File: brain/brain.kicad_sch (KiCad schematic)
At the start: 6 parts, among them J0 BAR0, J1 BAR1, J2 I2C, J5 XTRA, SW1 RESET, U1 Elite-C

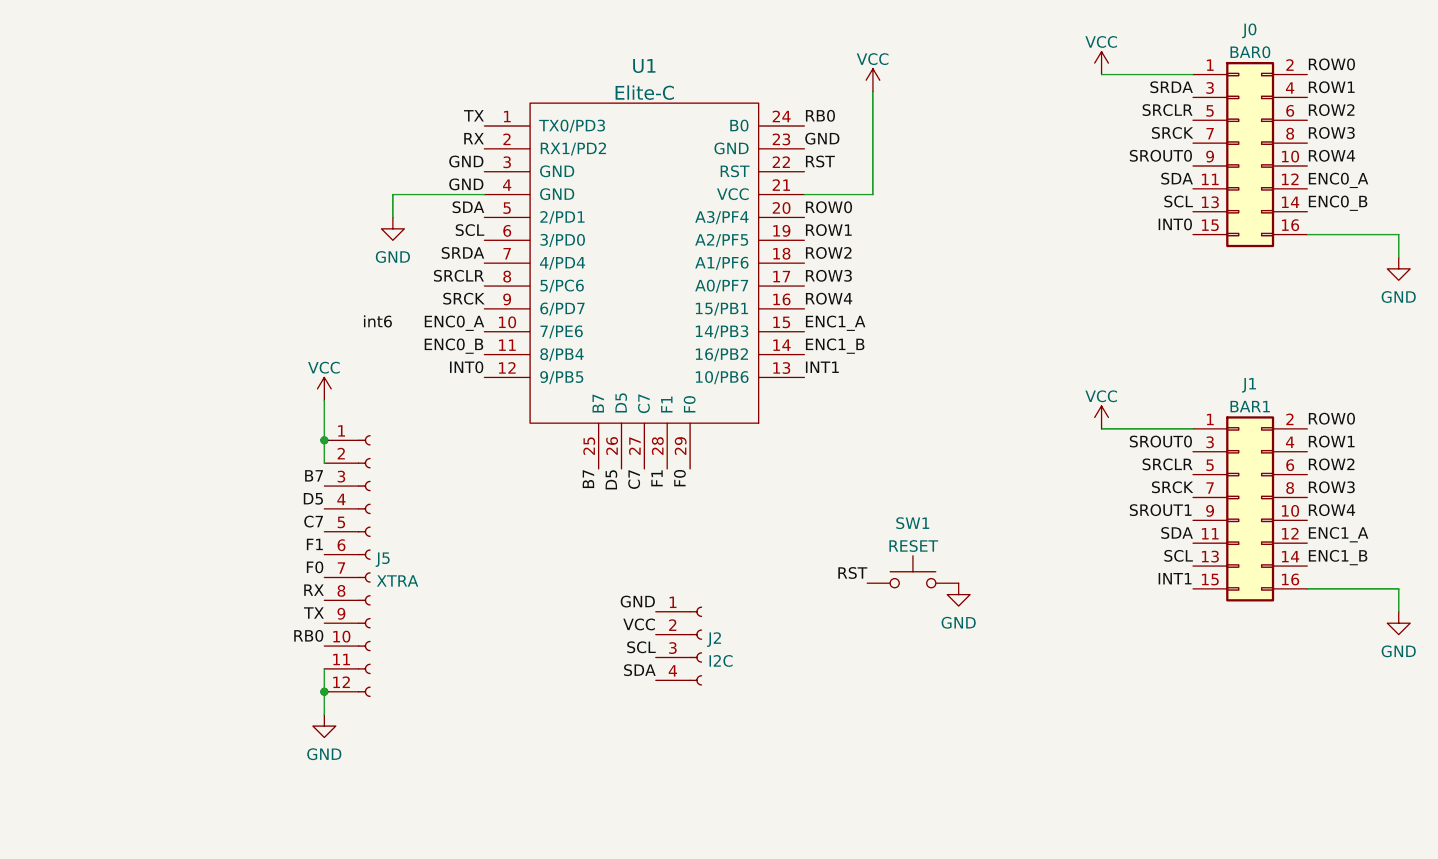
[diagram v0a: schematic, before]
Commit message: Use interrupt-enabled pins for encoder0 and int1
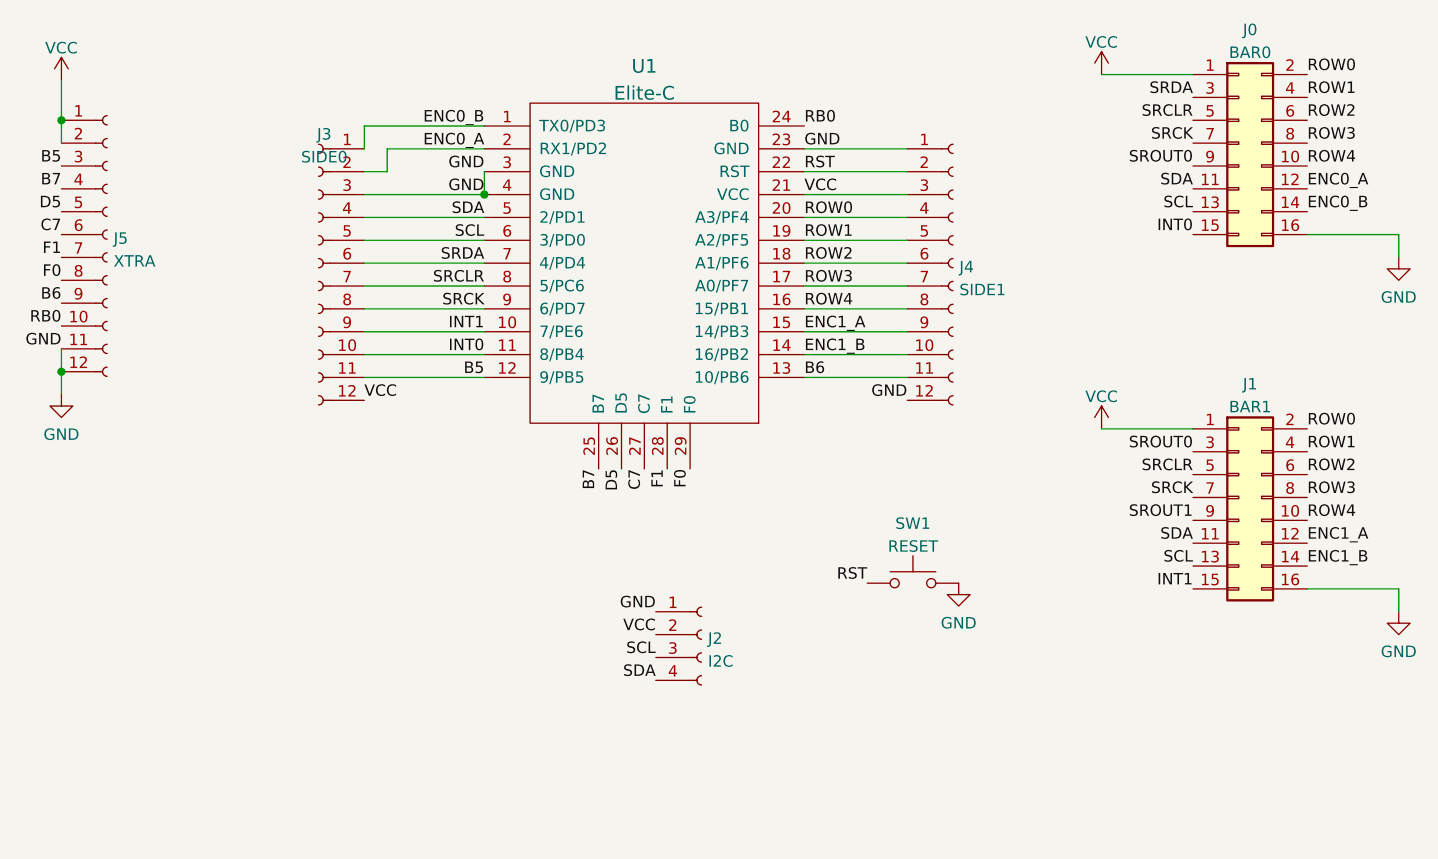
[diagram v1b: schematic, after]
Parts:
- added J3: SIDE0, Connector_PinSocket_2.54mm:PinSocket_1x12_P2.54mm_Vertical, symbol Connector:Conn_01x12_Female
- added J4: SIDE1, Connector_PinSocket_2.54mm:PinSocket_1x12_P2.54mm_Vertical, symbol Connector:Conn_01x12_Female
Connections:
- net B7: now also J5.4 (Pin_4); no longer J5.3 (Pin_3)
- net C7: now also J5.6 (Pin_6); no longer J5.5 (Pin_5)
- net D5: now also J5.5 (Pin_5); no longer J5.4 (Pin_4)
- net ENC0_A: now also U1.2 (RX1/PD2), J3.2 (Pin_2); no longer U1.10 (7/PE6)
- net ENC0_B: now also U1.1 (TX0/PD3), J3.1 (Pin_1); no longer U1.11 (8/PB4)
- net ENC1_A: now also J4.9 (Pin_9)
- net ENC1_B: now also J4.10 (Pin_10)
- net F0: now also J5.8 (Pin_8); no longer J5.7 (Pin_7)
- net F1: now also J5.7 (Pin_7); no longer J5.6 (Pin_6)
- net GND: now also J3.3 (Pin_3), J4.1 (Pin_1), J4.12 (Pin_12)
- net INT0: now also U1.11 (8/PB4), J3.10 (Pin_10); no longer U1.12 (9/PB5)
- net INT1: now also U1.10 (7/PE6), J3.9 (Pin_9); no longer U1.13 (10/PB6)
- net ROW0: now also J4.4 (Pin_4)
- net ROW1: now also J4.5 (Pin_5)
- net ROW2: now also J4.6 (Pin_6)
- net ROW3: now also J4.7 (Pin_7)
- net ROW4: now also J4.8 (Pin_8)
- net RST: now also J4.2 (Pin_2)
- net SCL: now also J3.5 (Pin_5)
- net SDA: now also J3.4 (Pin_4)
- net SRCK: now also J3.8 (Pin_8)
- net SRCLR: now also J3.7 (Pin_7)
- net SRDA: now also J3.6 (Pin_6)
- net VCC: now also J3.12 (Pin_12), J4.3 (Pin_3)
- removed net RX: J5.8 (Pin_8), U1.2 (RX1/PD2)
- net TX renamed B6
- net B6: now also U1.13 (10/PB6), J4.11 (Pin_11); no longer U1.1 (TX0/PD3)
- new net B5: J3.11 (Pin_11), J5.3 (Pin_3), U1.12 (9/PB5)
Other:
- moved on the sheet: J5

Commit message: Brain: Add mounting holes and silkscreen labels
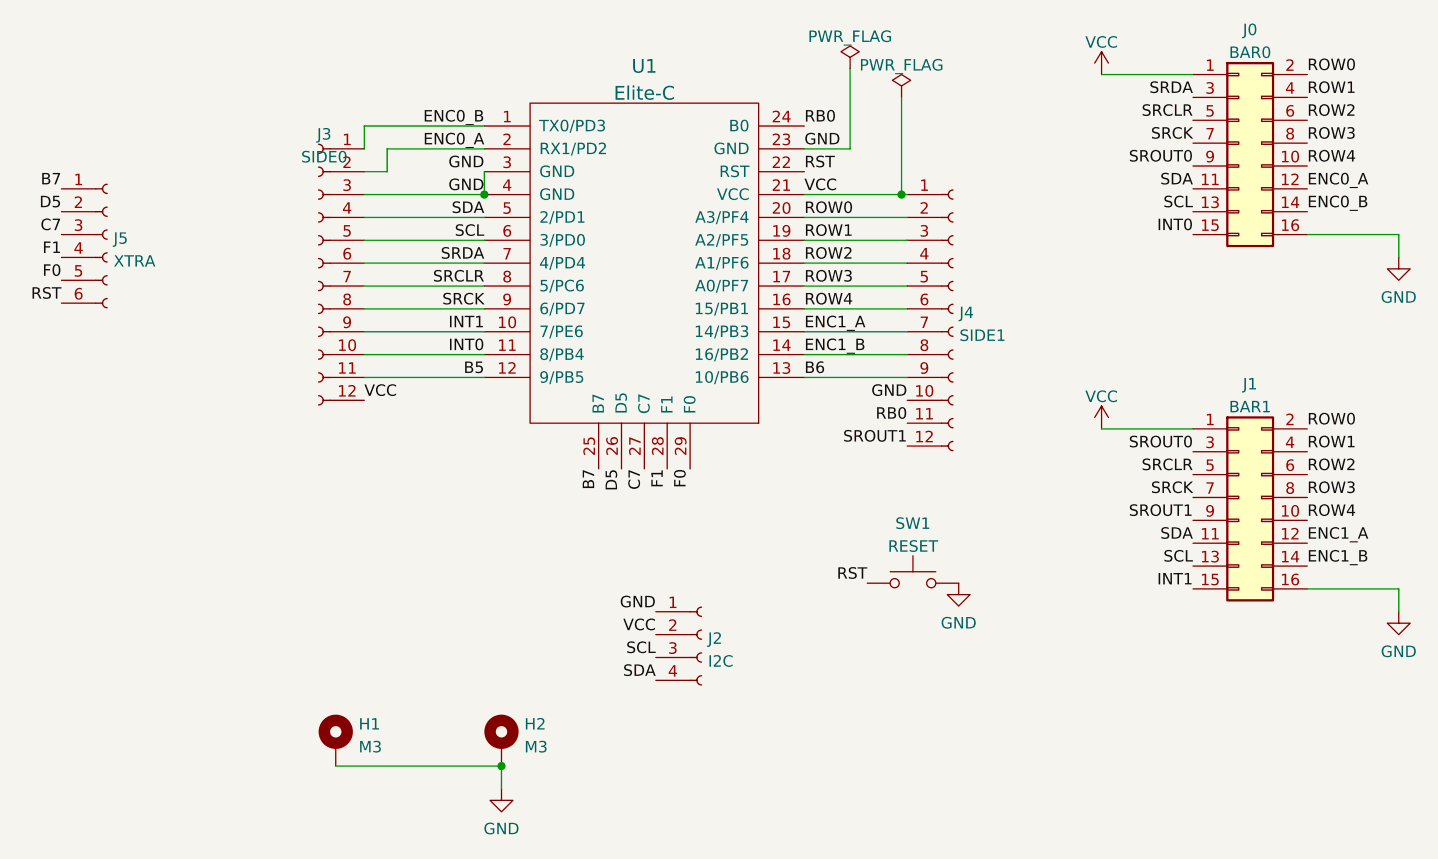
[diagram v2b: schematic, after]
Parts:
- added H1, H2: M3, MountingHole:MountingHole_3.2mm_M3_DIN965_Pad, symbol Mechanical:MountingHole_Pad
- J5: footprint Connector_PinSocket_2.54mm:PinSocket_1x12_P2.54mm_Vertical -> Connector_PinSocket_2.54mm:PinSocket_1x06_P2.54mm_Vertical; symbol Connector:Conn_01x12_Female -> Connector:Conn_01x06_Female
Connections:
- net B5: no longer J5.3 (Pin_3)
- net B6: now also J4.9 (Pin_9); no longer J4.11 (Pin_11), J5.9 (Pin_9)
- net B7: now also J5.1 (Pin_1); no longer J5.4 (Pin_4)
- net C7: now also J5.3 (Pin_3); no longer J5.6 (Pin_6)
- net D5: now also J5.2 (Pin_2); no longer J5.5 (Pin_5)
- net ENC1_A: now also J4.7 (Pin_7); no longer J4.9 (Pin_9)
- net ENC1_B: now also J4.8 (Pin_8); no longer J4.10 (Pin_10)
- net F0: now also J5.5 (Pin_5); no longer J5.8 (Pin_8)
- net F1: now also J5.4 (Pin_4); no longer J5.7 (Pin_7)
- net GND: now also J4.10 (Pin_10), H1.1, H2.1; no longer J4.1 (Pin_1), J4.12 (Pin_12), J5.11 (Pin_11), J5.12 (Pin_12)
- net RB0: now also J4.11 (Pin_11); no longer J5.10 (Pin_10)
- net ROW0: now also J4.2 (Pin_2); no longer J4.4 (Pin_4)
- net ROW1: now also J4.3 (Pin_3); no longer J4.5 (Pin_5)
- net ROW2: now also J4.4 (Pin_4); no longer J4.6 (Pin_6)
- net ROW3: now also J4.5 (Pin_5); no longer J4.7 (Pin_7)
- net ROW4: now also J4.6 (Pin_6); no longer J4.8 (Pin_8)
- net RST: now also J5.6 (Pin_6); no longer J4.2 (Pin_2)
- net SROUT1: now also J4.12 (Pin_12)
- net VCC: now also J4.1 (Pin_1); no longer J4.3 (Pin_3), J5.1 (Pin_1), J5.2 (Pin_2)
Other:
- moved on the sheet: J4
